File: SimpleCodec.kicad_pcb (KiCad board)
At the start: 4 copper layers, 59 x 95 mm, 93 parts, among them J1 RPI_ADC, J2 RP_GPIO, U1 AMS1117-5.0, U2 AMS1117-3.3, U3 MCP6002-xSN, U4 MCP6002-xSN, U5 CS4272, X1 PEDAL_COMBO_TOP

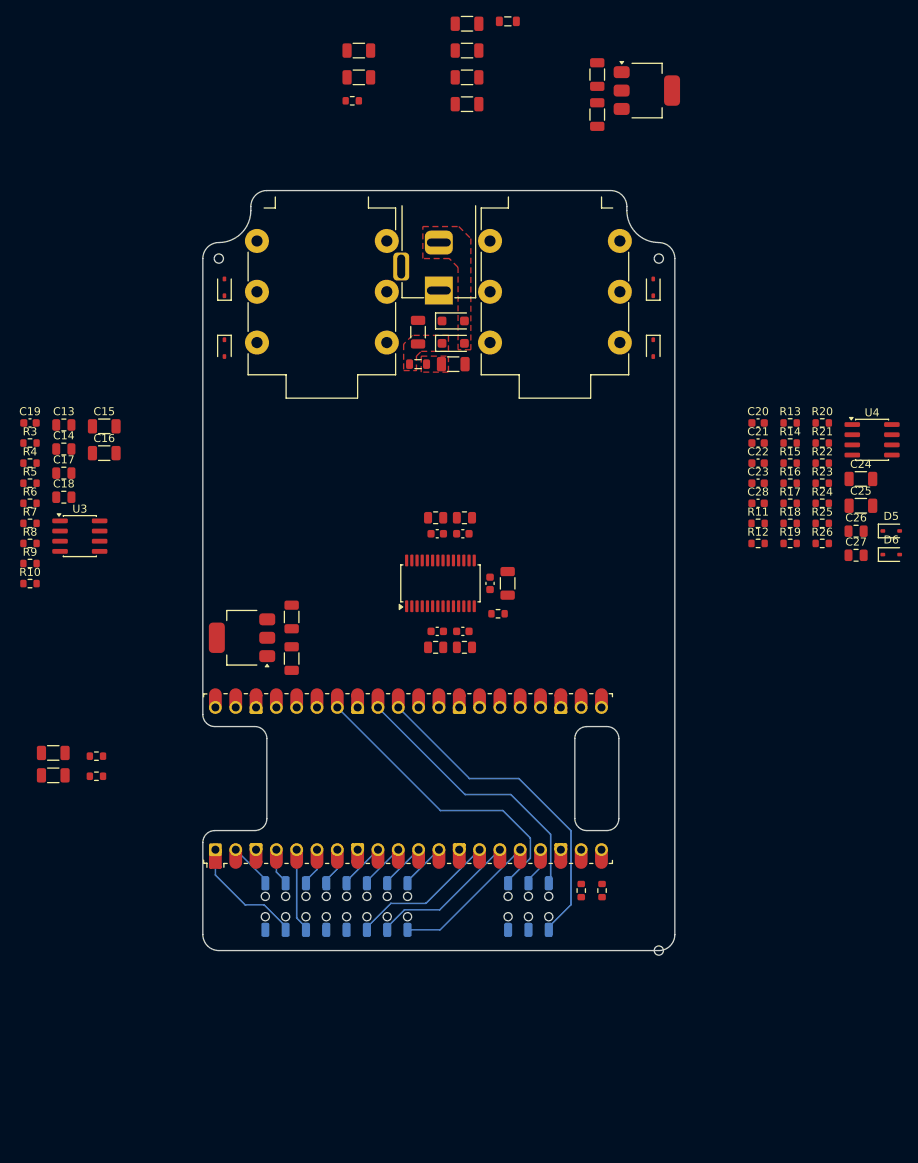
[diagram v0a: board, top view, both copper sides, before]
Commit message: Input buffer and power
Updated the input buffer layout.
Updated the power supply layout.
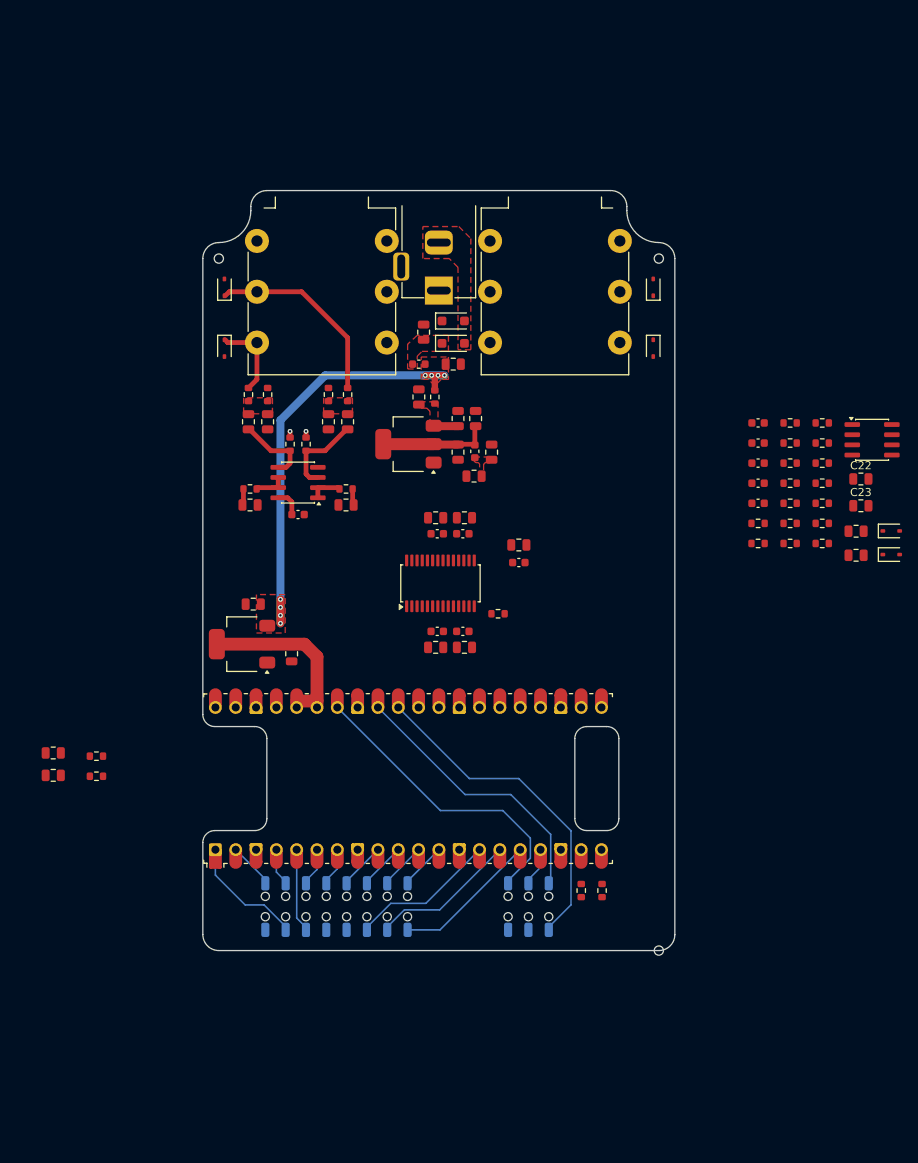
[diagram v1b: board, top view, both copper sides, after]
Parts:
- removed the C1 at (140.0, 25.0)
- removed the C10 at (153.5, 28.4)
- removed the C12 at (153.5, 31.7)
- removed the C7 at (153.5, 21.6)
- added C6: 10u, Capacitor_SMD:C_0805_2012Metric, F.Cu at (154.6, 71.0)
- added C8: 10u, Capacitor_SMD:C_0805_2012Metric, F.Cu at (156.6, 75.2)
- C1: renamed from C2; value 4.7u -> 10u; footprint Capacitor_SMD:C_1206_3216Metric -> Capacitor_SMD:C_0805_2012Metric
- C10: renamed from C11; footprint Capacitor_SMD:C_1206_3216Metric -> Capacitor_SMD:C_0805_2012Metric
- C13: renamed from C15; footprint Capacitor_SMD:C_1206_3216Metric -> Capacitor_SMD:C_0805_2012Metric
- C14: renamed from C16; footprint Capacitor_SMD:C_1206_3216Metric -> Capacitor_SMD:C_0805_2012Metric
- C2: renamed from C4; value 4.7u -> 10u; footprint Capacitor_SMD:C_1206_3216Metric -> Capacitor_SMD:C_0805_2012Metric
- C22: renamed from C24; footprint Capacitor_SMD:C_1206_3216Metric -> Capacitor_SMD:C_0805_2012Metric
- C23: renamed from C25; footprint Capacitor_SMD:C_1206_3216Metric -> Capacitor_SMD:C_0805_2012Metric
- C3: value 22u -> 10u; footprint Capacitor_SMD:C_1206_3216Metric -> Capacitor_SMD:C_0805_2012Metric
- C31: renamed from C33; value 10u -> 2.2n; footprint Capacitor_SMD:C_1206_3216Metric -> Capacitor_SMD:C_0805_2012Metric
- C35: renamed from C37; value 10u -> 2.2n; footprint Capacitor_SMD:C_1206_3216Metric -> Capacitor_SMD:C_0805_2012Metric
- C37: renamed from C39; value 22u -> 10u; footprint Capacitor_SMD:C_1206_3216Metric -> Capacitor_SMD:C_0805_2012Metric
- C4: renamed from C5; footprint Capacitor_SMD:C_1206_3216Metric -> Capacitor_SMD:C_0805_2012Metric
- C5: renamed from C6; footprint Capacitor_SMD:C_1206_3216Metric -> Capacitor_SMD:C_0805_2012Metric
- C7: renamed from C8; footprint Capacitor_SMD:C_1206_3216Metric -> Capacitor_SMD:C_0805_2012Metric
- C9: value 4.7u -> 10u; footprint Capacitor_SMD:C_1206_3216Metric -> Capacitor_SMD:C_0805_2012Metric
- FB1, FB2: footprint Inductor_SMD:L_0805_2012Metric -> Inductor_SMD:L_0603_1608Metric
- moved FB2 53.9 mm to (154.5, 75.1), turned to -90 degrees
- moved U1 53.3 mm to (146.2, 74.2), turned to 180 degrees
- moved C9 53.2 mm to (154.4, 78.2), turned to 180 degrees
- moved C4 46.1 mm to (147.5, 68.3)
- moved C5 45.6 mm to (152.4, 75.2)
- moved C3 44.4 mm to (152.4, 71.0), turned to 90 degrees
- moved R10 41.2 mm to (138.4, 79.8)
- moved R4 40.6 mm to (138.6, 68.0), turned to -90 degrees
- moved R6 39.7 mm to (136.2, 68.0), turned to 90 degrees
- moved R2 38.4 mm to (149.5, 68.3), turned to -90 degrees
- moved R8 36.7 mm to (133.4, 74.2), turned to 90 degrees
- moved C17 35.4 mm to (132.4, 83.0)
- moved C16 35.3 mm to (138.4, 81.8), turned to 180 degrees
- moved R7 34.0 mm to (131.4, 74.2), turned to 90 degrees
- moved C12 33.3 mm to (136.2, 71.4), turned to 90 degrees
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- renumbered C13 to C11, C14 to C12, C17 to C15, C18 to C16, C19 to C17, C20 to C18, C21 to C19, C22 to C20, C23 to C21, C26 to C24, C27 to C25, C28 to C26, C29 to C27, C30 to C28, C31 to C29, C32 to C30, C34 to C32, C35 to C33, C36 to C34, C38 to C36, C40 to C38
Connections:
- net Net-(C13-Pad2) renamed /Buffers_In/FILT_L
- net Net-(C14-Pad2) renamed /Buffers_In/FILT_R
- net Net-(R11-Pad2) renamed /Buffers_Out/FILT_LM
- net Net-(R12-Pad2) renamed /Buffers_Out/FILT_LP
- net Net-(R13-Pad2) renamed /Buffers_Out/FILT_RM
- net Net-(R14-Pad2) renamed /Buffers_Out/FILT_RP
- net Net-(U4A-+) renamed /Buffers_Out/OPP_L
- net Net-(U4A--) renamed /Buffers_Out/OPM_L
- net Net-(U4B-+) renamed /Buffers_Out/OPP_R
- net Net-(U4B--) renamed /Buffers_Out/OPM_R
- C13 pad 2: Net-(U3A-+) -> /Buffers_In/OPP_L
- C14 pad 2: Net-(U3B-+) -> /Buffers_In/OPP_R
- C20 pad 2: Net-(C22-Pad2) (its old number) -> /Buffers_Out/OPO_L
- C21 pad 2: Net-(C23-Pad2) (its old number) -> /Buffers_Out/OPO_R
- C22 pad 1: Net-(C22-Pad2) (its old number) -> /Buffers_Out/OPO_L
- C23 pad 1: Net-(C23-Pad2) (its old number) -> /Buffers_Out/OPO_R
- R10 pad 1: Net-(U3B--) -> /Buffers_In/OPM_R
- R21 pad 2: Net-(C22-Pad2) (its old number) -> /Buffers_Out/OPO_L
- R22 pad 2: Net-(C23-Pad2) (its old number) -> /Buffers_Out/OPO_R
- R7 pad 1: Net-(U3A-+) -> /Buffers_In/OPP_L
- R8 pad 1: Net-(U3B-+) -> /Buffers_In/OPP_R
- R9 pad 1: Net-(U3A--) -> /Buffers_In/OPM_L
- U3 pad 1: Net-(U3A--) -> /Buffers_In/OPM_R
- U3 pad 2: Net-(U3A--) -> /Buffers_In/OPM_R
- U3 pad 3: Net-(U3A-+) -> /Buffers_In/OPP_R
- U3 pad 5: Net-(U3B-+) -> /Buffers_In/OPP_L
- U3 pad 6: Net-(U3B--) -> /Buffers_In/OPM_L
- U3 pad 7: Net-(U3B--) -> /Buffers_In/OPM_L
- U4 pad 1: Net-(C22-Pad2) (its old number) -> /Buffers_Out/OPO_L
- U4 pad 7: Net-(C23-Pad2) (its old number) -> /Buffers_Out/OPO_R
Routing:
- net +VCC: track 0.00 -> 55.5 mm, vias 0 -> 8
- net /Buffers_In/AUDIO_INR: track 0.00 -> 24.2 mm
- net +3V3D: track 0.00 -> 21.3 mm
- net +5VA_RAW: track 0.00 -> 13.8 mm
- net /Buffers_In/OPP_R: track 0.00 -> 10.9 mm
- net /Buffers_In/AUDIO_INL: track 0.00 -> 10.2 mm
- net /Buffers_In/OPP_L: track 0.00 -> 9.56 mm
- net /Buffers_In/OPM_L: track 0.00 -> 4.04 mm
- net /Buffers_In/OPM_R: track 0.00 -> 4.04 mm
- net +VCC_FILT: track 0.00 -> 3.81 mm
- net +5VA: track 0.00 -> 3.49 mm
- net CODEC_INR: track 0.00 -> 2.05 mm
- net CODEC_INL: track 0.00 -> 2.05 mm
- net VCOM: track 0.00 -> 1.55 mm, vias 0 -> 2
- added copper zone on F.Cu, net +5VA
- added copper zone on F.Cu, net +VCC_FILT
- added copper zone on F.Cu, net /Buffers_In/FILT_L
- added copper zone on F.Cu, net /Buffers_In/FILT_R

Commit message: Codec layout
Updated the codec layout.
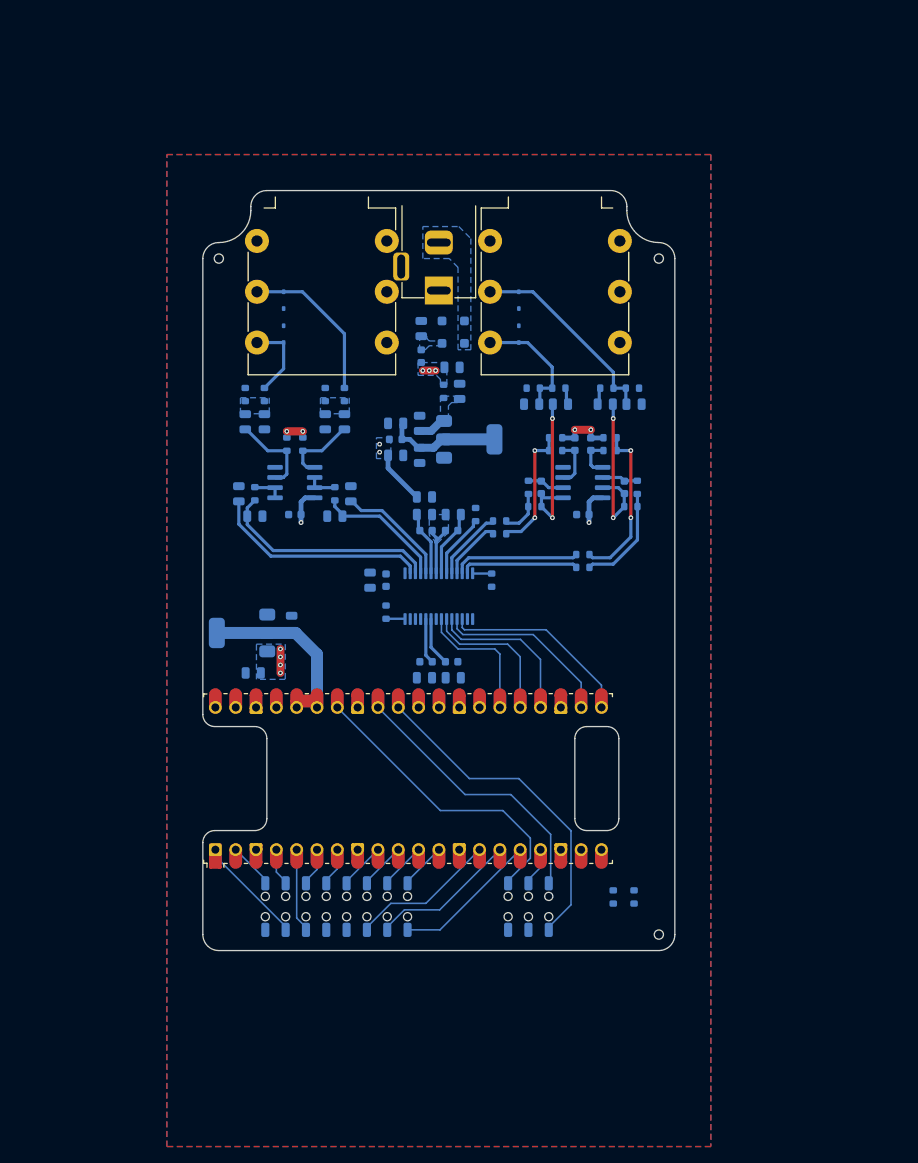
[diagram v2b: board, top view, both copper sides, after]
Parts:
- removed the D5 at (176.8, 62.2)
- removed the D6 at (176.8, 54.6)
- C1, C10, C11, C12, C13, C14, C15, C16, C17, C18, C19, C2, C20, C21, C22, C23, C24, C25, C26, C27, C28, C29, C3, C30, C31, C32, C33, C34, C35, C36, C37, C38, C4, C5, C6, C7, C8, C9, D1, D2, D3, D4, D5, D6, FB1, FB2, R1, R10, R11, R12, R13, R14, R15, R16, R17, R18, R19, R2, R20, R21, R22, R23, R24, R25, R26, R27, R28, R29, R3, R30, R4, R5, R6, R7, R8, R9, U1, U2, U3, U4, U5: moved to B.Cu
- moved R30 57.6 mm to (154.6, 83.0), turned to 90 degrees
- moved D6 56.4 mm to (160.0, 56.2), turned to -90 degrees
- moved R29 54.1 mm to (156.6, 91.2), turned to -90 degrees
- moved D5 52.7 mm to (160.0, 60.5), turned to 90 degrees
- moved C31 49.3 mm to (139.0, 80.4), turned to 90 degrees
- moved C24 43.6 mm to (161.6, 69.2), turned to 180 degrees
- moved C35 42.2 mm to (125.0, 80.4), turned to 90 degrees
- moved R25 39.9 mm to (161.8, 67.2), turned to 180 degrees
- moved C22 38.7 mm to (165.2, 69.2)
- moved R21 36.8 mm to (162.0, 82.0)
- moved U4 36.5 mm to (168.0, 79.0)
- moved R23 35.0 mm to (165.0, 67.2), turned to 180 degrees
- moved C23 34.4 mm to (170.8, 69.2), turned to 180 degrees
- moved C25 33.6 mm to (174.4, 69.2)
- moved R17 32.8 mm to (161.2, 79.6), turned to 90 degrees
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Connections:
- C11 pad 2: /Buffers_In/FILT_L -> /Buffers_In/FILT_R
- C12 pad 2: /Buffers_In/FILT_R -> /Buffers_In/FILT_L
- C13 pad 1: /Buffers_In/FILT_L -> /Buffers_In/FILT_R
- C13 pad 2: /Buffers_In/OPP_L -> /Buffers_In/OPP_R
- C14 pad 1: /Buffers_In/FILT_R -> /Buffers_In/FILT_L
- C14 pad 2: /Buffers_In/OPP_R -> /Buffers_In/OPP_L
- C15 pad 1: CODEC_INL -> CODEC_INR
- C16 pad 1: CODEC_INR -> CODEC_INL
- R10 pad 1: /Buffers_In/OPM_R -> /Buffers_In/OPM_L
- R10 pad 2: CODEC_INR -> CODEC_INL
- R3 pad 1: /Buffers_In/AUDIO_INL -> /Buffers_In/AUDIO_INR
- R3 pad 2: /Buffers_In/FILT_L -> /Buffers_In/FILT_R
- R4 pad 1: /Buffers_In/AUDIO_INR -> /Buffers_In/AUDIO_INL
- R4 pad 2: /Buffers_In/FILT_R -> /Buffers_In/FILT_L
- R5 pad 1: /Buffers_In/FILT_L -> /Buffers_In/FILT_R
- R6 pad 1: /Buffers_In/FILT_R -> /Buffers_In/FILT_L
- R7 pad 1: /Buffers_In/OPP_L -> /Buffers_In/OPP_R
- R8 pad 1: /Buffers_In/OPP_R -> /Buffers_In/OPP_L
- R9 pad 1: /Buffers_In/OPM_L -> /Buffers_In/OPM_R
- R9 pad 2: CODEC_INL -> CODEC_INR
- U3 pad 1: /Buffers_In/OPM_R -> /Buffers_In/OPM_L
- U3 pad 2: /Buffers_In/OPM_R -> /Buffers_In/OPM_L
- U3 pad 3: /Buffers_In/OPP_R -> /Buffers_In/OPP_L
- U3 pad 5: /Buffers_In/OPP_L -> /Buffers_In/OPP_R
- U3 pad 6: /Buffers_In/OPM_L -> /Buffers_In/OPM_R
- U3 pad 7: /Buffers_In/OPM_L -> /Buffers_In/OPM_R
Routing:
- net +VCC: track 55.5 -> 4.60 mm, vias 8 -> 7
- net /Codec/INL-: track 0.00 -> 27.4 mm
- net CODEC_INL: track 2.05 -> 27.7 mm
- net /Buffers_Out/AUDIO_OUTR: track 0.00 -> 25.1 mm
- net I2S_MCLK: track 0.00 -> 24.2 mm
- net I2S_LRCK: track 0.00 -> 22.6 mm
- net /Buffers_Out/OPO_R: track 0.00 -> 20.9 mm, vias 0 -> 2
- net /Buffers_Out/FILT_RP: track 0.00 -> 20.6 mm, vias 0 -> 2
- net /Buffers_Out/OPO_L: track 0.00 -> 20.4 mm, vias 0 -> 2
- net I2S_SCLK: track 0.00 -> 20.0 mm
- net +5VA: track 3.49 -> 23.4 mm, vias 0 -> 4
- net I2S_SDOUT: track 0.00 -> 18.4 mm
- net I2S_SDIN: track 0.00 -> 16.8 mm
- net /Buffers_Out/FILT_LP: track 0.00 -> 16.1 mm, vias 0 -> 2
- net CODEC_OUTR+: track 0.00 -> 15.9 mm
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- added copper zone on B.Cu, net +5VA
- added copper zone on B.Cu, net +VCC
- added copper zone on B.Cu, net +VCC_FILT
- added copper zone on B.Cu, net +VDC
- added copper zone on B.Cu, net +VDC_PROT
- added copper zone on B.Cu, net /Buffers_In/FILT_L
- added copper zone on B.Cu, net /Buffers_In/FILT_R
- added copper zone on B.Cu, net GND
- added copper zone on F.Cu, net GND
- removed copper zone on F.Cu, net +5VA
- removed copper zone on F.Cu, net +VCC
- removed copper zone on F.Cu, net +VCC_FILT
- removed copper zone on F.Cu, net +VDC
- removed copper zone on F.Cu, net +VDC_PROT
- removed copper zone on F.Cu, net /Buffers_In/FILT_L
- removed copper zone on F.Cu, net /Buffers_In/FILT_R

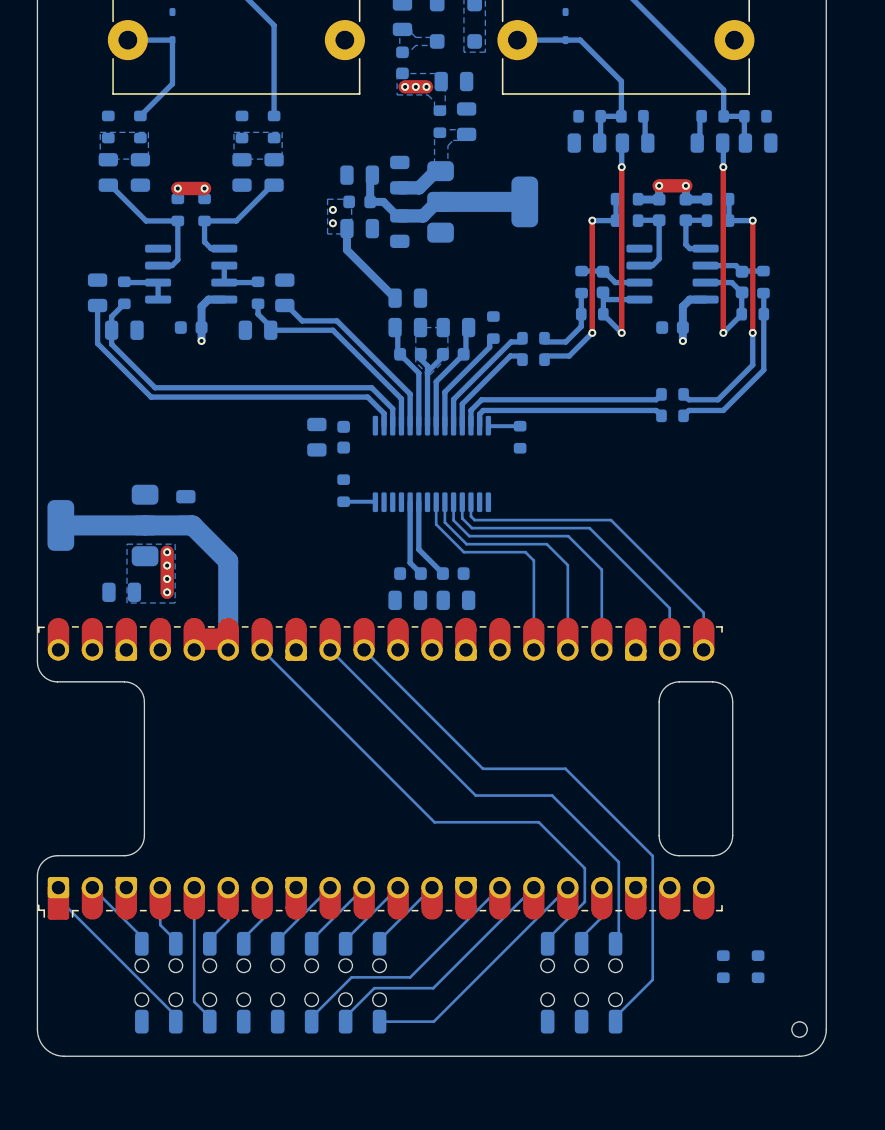
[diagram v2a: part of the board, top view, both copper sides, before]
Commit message: Missing connections
Updated the board layout.
Added al missing connections.
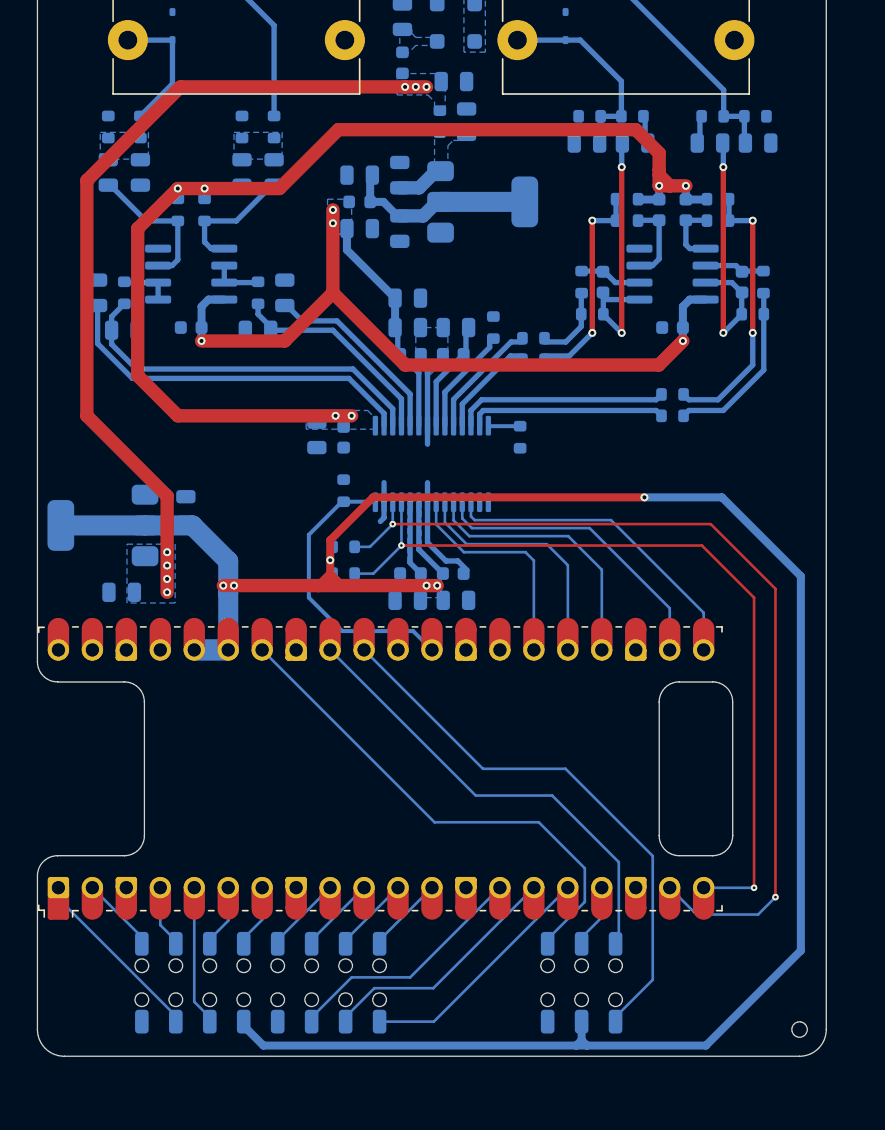
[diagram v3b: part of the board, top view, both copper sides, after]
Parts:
- moved R27 42.7 mm to (143.4, 101.4), turned to 0 degrees
- moved R28 42.3 mm to (143.4, 99.4), turned to 0 degrees
- moved C37 0.17 mm to (141.4, 91.0)
- renumbered C12 to C11, C11 to C12, C14 to C13, C13 to C14, C16 to C15, C15 to C16, R9 to R10, R4 to R3, R3 to R4, R6 to R5, R5 to R6, R8 to R7, R7 to R8, R10 to R9
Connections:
- A1 pad 27: CODEC_RST -> unconnected-(A1-GPIO21-Pad27)
- A1 pad 29: unconnected-(A1-GPIO22-Pad29)_1 -> CODEC_RST
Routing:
- net +3V3D: track 34.6 -> 172.8 mm, vias 0 -> 6
- net VCOM: track 10.8 -> 83.4 mm, vias 4 -> 6
- net I2C_SDA: track 0.00 -> 68.2 mm, vias 0 -> 2
- net I2C_SCL: track 0.00 -> 61.2 mm, vias 0 -> 2
- net +VCC: track 4.60 -> 61.6 mm
- net +5VA: track 23.4 -> 72.3 mm
- net CODEC_RST: track 2.34 -> 21.5 mm
- net GND: track 7.55 -> 20.2 mm
- added copper zone on B.Cu, net +3V3D
- added copper zone on B.Cu, net VCOM
